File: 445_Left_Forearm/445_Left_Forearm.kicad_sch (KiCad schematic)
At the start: 2 parts, among them J1 69167-107HLF, U1 LSM6DSMTR

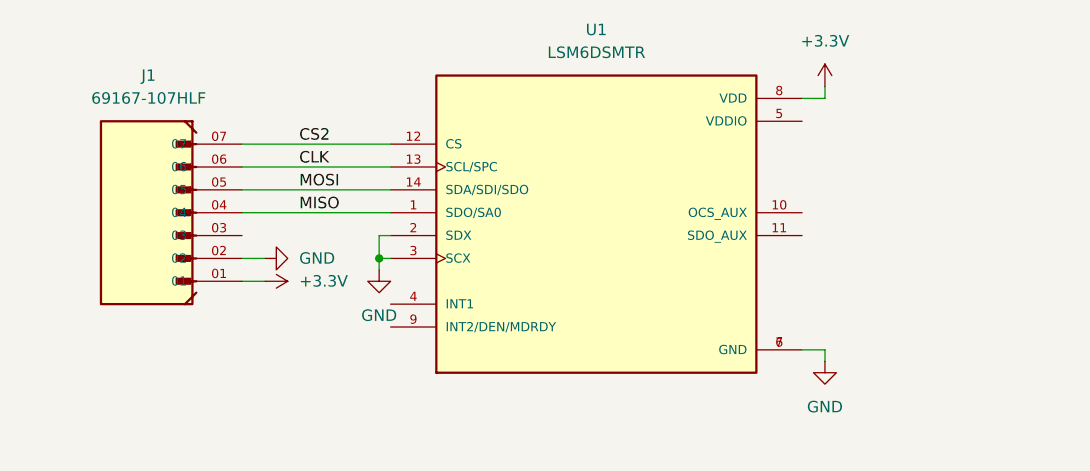
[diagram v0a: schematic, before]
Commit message: Added filtering caps and int line
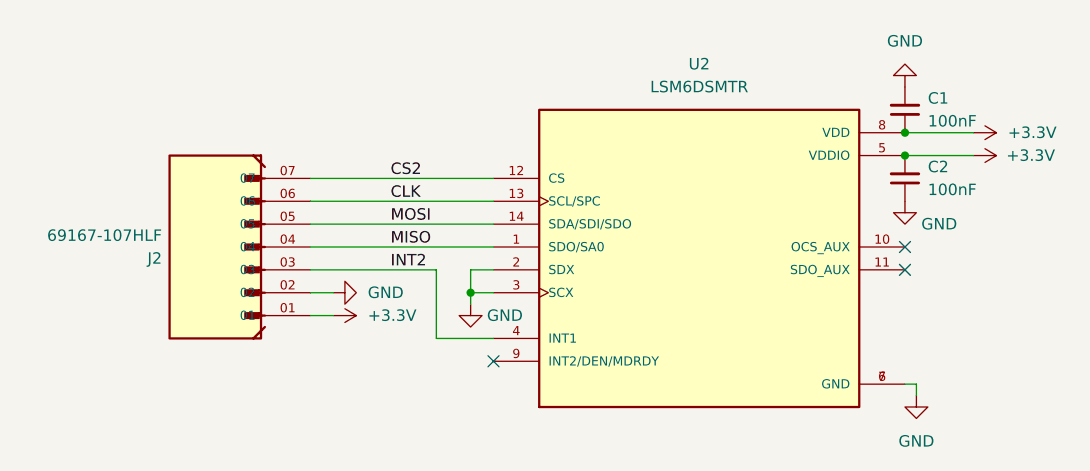
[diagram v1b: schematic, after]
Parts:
- removed J1: 69167-107HLF, 69167-107HLF:AMPHENOL_69167-107HLF, symbol 69167-107HLF:69167-107HLF
- removed U1: LSM6DSMTR, LSM6DSMTR (1):PQFN50P300X250X86-14N, symbol LSM6DSMTR:LSM6DSMTR
- added C1, C2: 100nF, symbol Device:C_Small
- added J2: 69167-107HLF, 69167-107HLF:AMPHENOL_69167-107HLF, symbol 69167-107HLF:69167-107HLF
- added U2: LSM6DSMTR, LSM6DSMTR (1):PQFN50P300X250X86-14N, symbol LSM6DSMTR:LSM6DSMTR
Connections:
- net +3.3V: now also C1.1, C2.2, J2.01, U2.5 (VDDIO), U2.8 (VDD)
- net CLK: now also J2.06, U2.13 (SCL/SPC)
- net CS2: now also J2.07, U2.12 (CS)
- net GND: now also C1.2, C2.1, J2.02, U2.2 (SDX), U2.3 (SCX), U2.6 (GND), U2.7 (GND)
- net MISO: now also J2.04, U2.1 (SDO/SA0)
- net MOSI: now also J2.05, U2.14 (SDA/SDI/SDO)
- new net INT2: J2.03, U2.4 (INT1)
- no-connect marks 0 -> 3

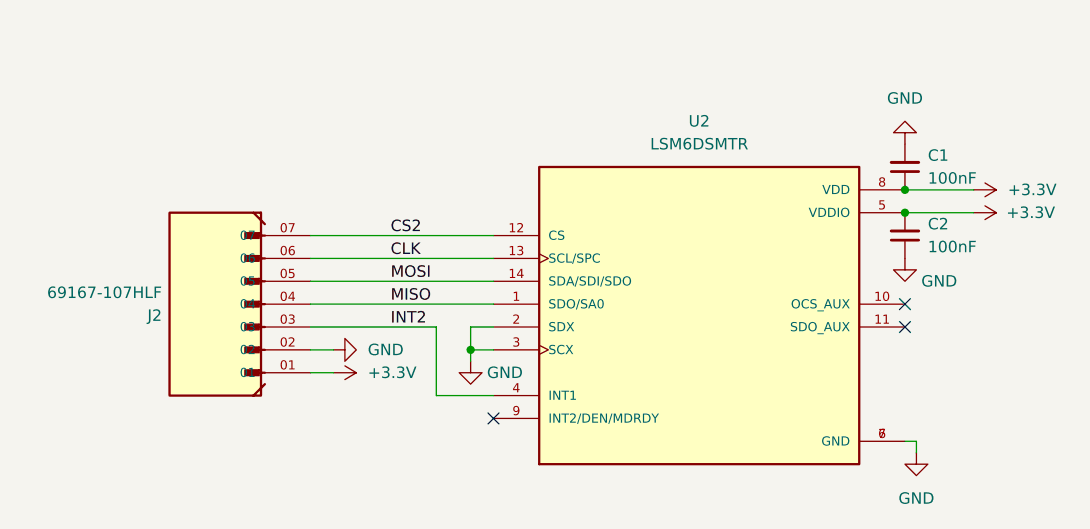
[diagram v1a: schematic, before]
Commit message: enable signal and analog switches
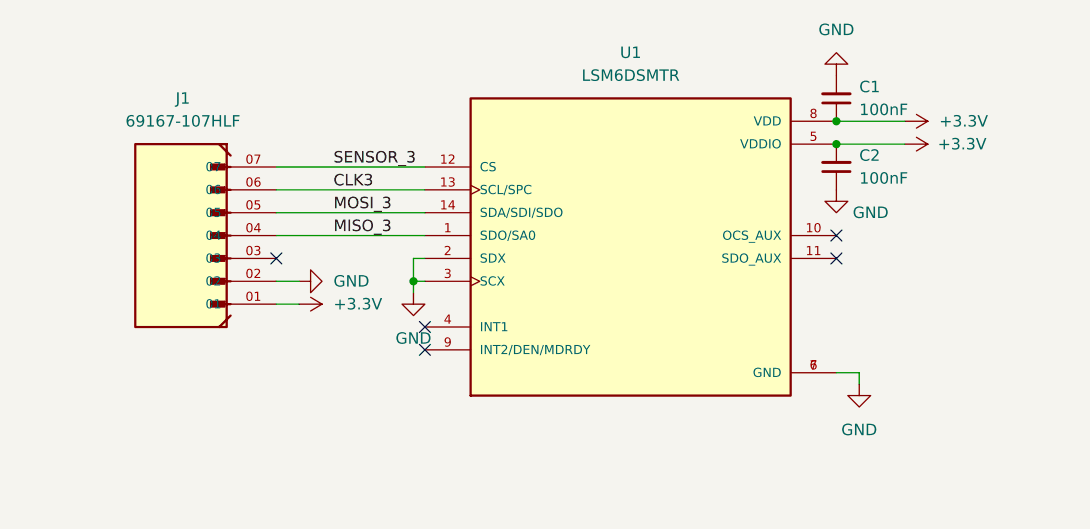
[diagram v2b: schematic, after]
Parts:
- removed J2: 69167-107HLF, 69167-107HLF:AMPHENOL_69167-107HLF, symbol 69167-107HLF:69167-107HLF
- removed U2: LSM6DSMTR, LSM6DSMTR (1):PQFN50P300X250X86-14N, symbol LSM6DSMTR:LSM6DSMTR
- added J1: 69167-107HLF, 69167-107HLF:AMPHENOL_69167-107HLF, symbol 69167-107HLF:69167-107HLF
- added U1: LSM6DSMTR, LSM6DSMTR (1):PQFN50P300X250X86-14N, symbol LSM6DSMTR:LSM6DSMTR
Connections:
- net +3.3V: now also J1.01, U1.5 (VDDIO), U1.8 (VDD)
- net GND: now also J1.02, U1.2 (SDX), U1.3 (SCX), U1.6 (GND), U1.7 (GND)
- new net CLK3: J1.06, U1.13 (SCL/SPC)
- new net MISO_3: J1.04, U1.1 (SDO/SA0)
- new net MOSI_3: J1.05, U1.14 (SDA/SDI/SDO)
- new net SENSOR_3: J1.07, U1.12 (CS)
- no-connect marks 3 -> 5

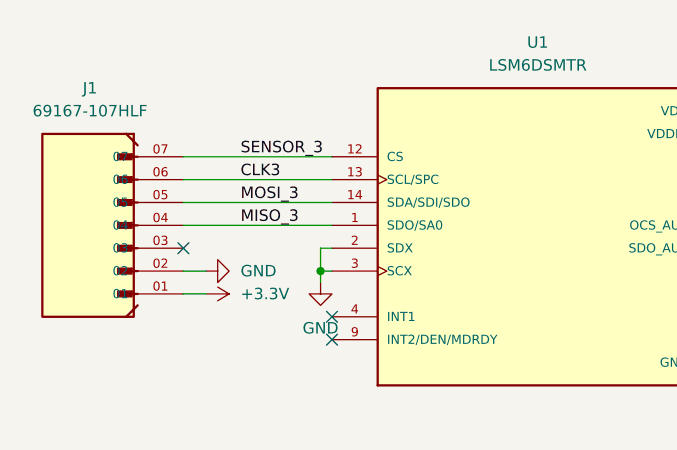
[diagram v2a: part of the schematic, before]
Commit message: replace bicep connector and add int1 connections
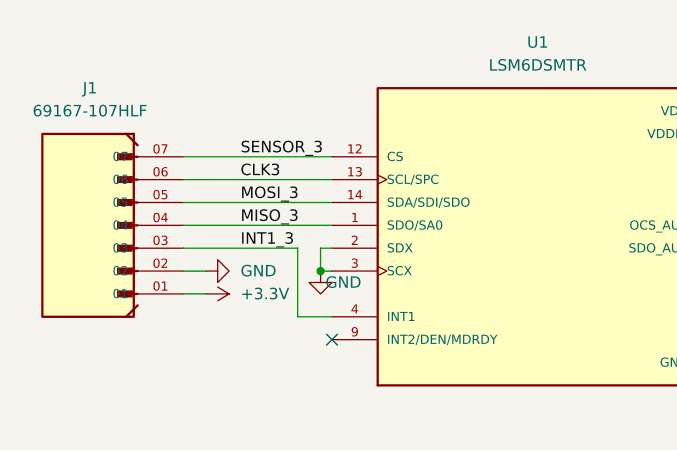
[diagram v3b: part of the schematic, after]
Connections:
- net INT1_3: now reaches J1.03
- net INT1_3: now also U1.4 (INT1)
- no-connect marks 5 -> 3
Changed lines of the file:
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@@
   )
   (no_connect (at 140.97 105.41))
-  (no_connect (at 140.97 102.87))
   (no_connect (at 186.69 92.71))
-  (no_connect (at 124.46 95.25))
   (no_connect (at 186.69 95.25))
   (wire (pts (xy 124.46 90.17) (xy 140.97 90.17))
@@
     (stroke (width 0) (type default))
   )
-  (wire (pts (xy 139.7 99.06) (xy 139.7 97.79))
+  (wire (pts (xy 137.16 95.25) (xy 137.16 102.87))
     (stroke (width 0) (type default))
   )
@@
     (stroke (width 0) (type default))
   )
+  (wire (pts (xy 124.46 95.25) (xy 137.16 95.25))
+    (stroke (width 0) (type default))
+  )
   (wire (pts (xy 124.46 97.79) (xy 127 97.79))
     (stroke (width 0) (type default))
@@
   )
   (wire (pts (xy 139.7 95.25) (xy 140.97 95.25))
+    (stroke (width 0) (type default))
+  )
+  (wire (pts (xy 137.16 102.87) (xy 140.97 102.87))
     (stroke (width 0) (type default))
   )
@@
   )
   (label "SENSOR_3" (at 130.81 85.09 0) (fields_autoplaced)
+    (effects (font (size 1.27 1.27)) (justify left bottom))
+  )
+  (label "INT1_3" (at 130.81 95.25 0) (fields_autoplaced)
     (effects (font (size 1.27 1.27)) (justify left bottom))
   )
@@
     )
   )
-  (symbol (lib_id "power:GND") (at 139.7 99.06 0) (unit 1)
-    (in_bom yes) (on_board yes) (dnp no) (fields_autoplaced)
-    (property "Reference" "#PWR03" (at 139.7 105.41 0)
-      (effects (font (size 1.27 1.27)) hide)
-    )
-    (property "Value" "GND" (at 139.7 104.14 0)
-      (effects (font (size 1.27 1.27)))
-    )
-    (property "Footprint" "" (at 139.7 99.06 0)
-      (effects (font (size 1.27 1.27)) hide)
-    )
-    (property "Datasheet" "" (at 139.7 99.06 0)
-      (effects (font (size 1.27 1.27)) hide)
-    )
+  (symbol (lib_id "power:GND") (at 139.7 97.79 0) (unit 1)
+    (in_bom yes) (on_board yes) (dnp no)
+    (property "Reference" "#PWR03" (at 139.7 104.14 0)
+      (effects (font (size 1.27 1.27)) hide)
+    )
+    (property "Value" "GND" (at 142.24 99.06 0)
+      (effects (font (size 1.27 1.27)))
+    )
+    (property "Footprint" "" (at 139.7 97.79 0)
+      (effects (font (size 1.27 1.27)) hide)
+    )
+    (property "Datasheet" "" (at 139.7 97.79 0)
+      (effects (font (size 1.27 1.27)) hide)
+    )

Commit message: Layout First Draft
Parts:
- added H1, H2, H3, H4: MountingHole, MountingHole:MountingHole_2mm, symbol Mechanical:MountingHole
- C1, C2: footprint (none) -> CL21F104ZAANNNC:CAPC2012X135N
- renumbered J1 to J6, U1 to U5
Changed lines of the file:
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@@
       (effects (font (size 1.27 1.27)) (justify right))
     )
-    (property "Footprint" "" (at 186.69 85.09 0)
+    (property "Footprint" "CL21F104ZAANNNC:CAPC2012X135N" (at 186.69 85.09 0)
       (effects (font (size 1.27 1.27)) hide)
     )
@@
   (symbol (lib_id "69167-107HLF:69167-107HLF") (at 114.3 92.71 180) (unit 1)
     (in_bom yes) (on_board yes) (dnp no) (fields_autoplaced)
-    (property "Reference" "J1" (at 114.0835 77.47 0)
+    (property "Reference" "J6" (at 114.0835 77.47 0)
       (effects (font (size 1.27 1.27)))
     )
@@
       (project "445_Left_Forearm"
         (path "/938e853c-b9ff-4ba2-80b9-98a9065fc92f"
-          (reference "J1") (unit 1)
+          (reference "J6") (unit 1)
         )
       )
@@
       (effects (font (size 1.27 1.27)) (justify right))
     )
-    (property "Footprint" "" (at 186.69 77.47 0)
+    (property "Footprint" "CL21F104ZAANNNC:CAPC2012X135N" (at 186.69 77.47 0)
       (effects (font (size 1.27 1.27)) hide)
     )
@@
         (path "/938e853c-b9ff-4ba2-80b9-98a9065fc92f"
           (reference "C1") (unit 1)
+        )
+      )
+    )
+  )
+  (symbol (lib_id "Mechanical:MountingHole") (at 25.4 54.61 0) (unit 1)
+    (in_bom yes) (on_board yes) (dnp no) (fields_autoplaced)
+    (property "Reference" "H4" (at 27.94 53.34 0)
+      (effects (font (size 1.27 1.27)) (justify left))
+    )
+    (property "Value" "MountingHole" (at 27.94 55.88 0)
+      (effects (font (size 1.27 1.27)) (justify left))
+    )
+    (property "Footprint" "MountingHole:MountingHole_2mm" (at 25.4 54.61 0)
+      (effects (font (size 1.27 1.27)) hide)
+    )
+    (property "Datasheet" "~" (at 25.4 54.61 0)
+      (effects (font (size 1.27 1.27)) hide)
+    )
+    (instances
+      (project "445_Left_Forearm"
+        (path "/938e853c-b9ff-4ba2-80b9-98a9065fc92f"
+          (reference "H4") (unit 1)
         )
       )
@@
   (symbol (lib_id "LSM6DSMTR:LSM6DSMTR") (at 163.83 92.71 0) (unit 1)
     (in_bom yes) (on_board yes) (dnp no) (fields_autoplaced)
-    (property "Reference" "U1" (at 163.83 72.39 0)
+    (property "Reference" "U5" (at 163.83 72.39 0)
       (effects (font (size 1.27 1.27)))
     )
@@
       (project "445_Left_Forearm"
         (path "/938e853c-b9ff-4ba2-80b9-98a9065fc92f"
-          (reference "U1") (unit 1)
+          (reference "U5") (unit 1)
         )
       )
@@
         )
       )
+    )
+  )
+  (symbol (lib_id "Mechanical:MountingHole") (at 25.4 44.45 0) (unit 1)
+    (in_bom yes) (on_board yes) (dnp no) (fields_autoplaced)
+    (property "Reference" "H3" (at 27.94 43.18 0)
+      (effects (font (size 1.27 1.27)) (justify left))
+    )
+    (property "Value" "MountingHole" (at 27.94 45.72 0)
+      (effects (font (size 1.27 1.27)) (justify left))
+    )
+    (property "Footprint" "MountingHole:MountingHole_2mm" (at 25.4 44.45 0)
+      (effects (font (size 1.27 1.27)) hide)
+    )
+    (property "Datasheet" "~" (at 25.4 44.45 0)
+      (effects (font (size 1.27 1.27)) hide)
+    )
+    (instances
+      (project "445_Left_Forearm"
+        (path "/938e853c-b9ff-4ba2-80b9-98a9065fc92f"
+          (reference "H3") (unit 1)
+        )
+      )
+    )
+  )
+  (symbol (lib_id "Mechanical:MountingHole") (at 25.4 25.4 0) (unit 1)
+    (in_bom yes) (on_board yes) (dnp no) (fields_autoplaced)
+    (property "Reference" "H1" (at 27.94 24.13 0)
+      (effects (font (size 1.27 1.27)) (justify left))
+    )
+    (property "Value" "MountingHole" (at 27.94 26.67 0)
+      (effects (font (size 1.27 1.27)) (justify left))
+    )
+    (property "Footprint" "MountingHole:MountingHole_2mm" (at 25.4 25.4 0)
+      (effects (font (size 1.27 1.27)) hide)
+    )
+    (property "Datasheet" "~" (at 25.4 25.4 0)
+      (effects (font (size 1.27 1.27)) hide)
+    )
+    (instances
+      (project "445_Left_Forearm"
+        (path "/938e853c-b9ff-4ba2-80b9-98a9065fc92f"
+          (reference "H1") (unit 1)
+        )
+      )
+    )
+  )
+  (symbol (lib_id "Mechanical:MountingHole") (at 25.4 34.29 0) (unit 1)
+    (in_bom yes) (on_board yes) (dnp no) (fields_autoplaced)
+    (property "Reference" "H2" (at 27.94 33.02 0)
+      (effects (font (size 1.27 1.27)) (justify left))
+    )
+    (property "Value" "MountingHole" (at 27.94 35.56 0)
+      (effects (font (size 1.27 1.27)) (justify left))
+    )
+    (property "Footprint" "MountingHole:MountingHole_2mm" (at 25.4 34.29 0)
+      (effects (font (size 1.27 1.27)) hide)
+    )
+    (property "Datasheet" "~" (at 25.4 34.29 0)
+      (effects (font (size 1.27 1.27)) hide)
+    )
+    (instances
+      (project "445_Left_Forearm"
+        (path "/938e853c-b9ff-4ba2-80b9-98a9065fc92f"
+          (reference "H2") (unit 1)
+        )
+      )
